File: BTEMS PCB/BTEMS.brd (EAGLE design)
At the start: 44.5 x 63.5 mm, 22 parts

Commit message: Solidified part position, added BOM
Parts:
- removed U$1: SDMMC06132, adafruit:06132
- added SDSLOT: SDMMC06132, adafruit:06132
- ARDUINO_A4-5, ARDUINO_A6-7: device SparkFun-Connectors:1X02_LOCK -> SparkFun-Connectors:1X02
- BAT_HEADER: device SparkFun-Connectors:SCREWTERMINAL-3.5MM-2_LOCK -> SparkFun-Connectors:1X02_2.54_SCREWTERM
- EXHEADER_A4-5, EXHEADER_A6-7: device SparkFun-Connectors:1X02 -> SparkFun-Connectors:1X02_LOCK
- I2C_R1, I2C_R2: value (none) -> 2.2k
- RTC_HEADER: device SparkFun-Connectors:1X04_LOCK -> SparkFun-Connectors:1X06_FEMALE_LOCK.010
- moved BAT_HEADER 54.5 mm to (4.19, 15.5)
- moved S1 42.1 mm to (3.68, 26.2), turned to 180 degrees
- moved MLX_HEADER 35.6 mm to (39.4, 2.54), turned to 180 degrees
- moved I2C_R2 25.0 mm to (20.3, 14.0), turned to 180 degrees
- moved ARDUINO_A6-7 24.1 mm to (30.6, 22.5)
- moved EXHEADER_A0-3 21.7 mm to (11.4, 27.9)
- moved EXHEADER_D2-9 21.7 mm to (11.4, 7.62)
- moved RED_LED 18.8 mm to (43.6, 26.3), turned to 90 degrees
- moved GREEN_LED 18.7 mm to (47.9, 26.3), turned to 90 degrees
- moved ARDUINO_A0-3 17.0 mm to (11.4, 25.4)
- moved ARDUINO_D2-9 17.0 mm to (11.4, 10.2)
- moved R3 16.6 mm to (35.4, 31.8), turned to 180 degrees
- moved R4 16.2 mm to (45.0, 31.8), turned to 180 degrees
- moved I2C_R1 15.5 mm to (30.5, 14.0), turned to 0 degrees
- moved EXHEADER_A6-7 11.5 mm to (24.1, 2.54), turned to 90 degrees
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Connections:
- net 3.3V: now also RTC_HEADER.2, RTC_HEADER.5, SDSLOT.4; no longer U$1.4
- net BAT_IN: now also BAT_HEADER.P2; no longer BAT_HEADER.2
- net D11: now also SDSLOT.2; no longer U$1.2
- net D12: now also SDSLOT.7; no longer U$1.7
- net D13: now also SDSLOT.5; no longer U$1.5
- net D4: now also SDSLOT.1; no longer U$1.1
- net GND: now also BAT_HEADER.P1, RTC_HEADER.6, SDSLOT.3, SDSLOT.6, SDSLOT.GP, SDSLOT.GP3; no longer BAT_HEADER.1, U$1.3, U$1.6, U$1.GP, U$1.GP3
- net VCC: no longer RTC_HEADER.2
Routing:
- net RST: track 5.08 -> 0.00 mm
- net GND: track 5.08 -> 0.00 mm
- net RXI: track 2.67 -> 0.00 mm
- net D9: track 2.67 -> 0.00 mm
- net D7: track 2.67 -> 0.00 mm
- net D5: track 2.67 -> 0.00 mm
- net D3: track 2.67 -> 0.00 mm
- net RAW: track 2.67 -> 0.00 mm
- net D13: track 2.67 -> 0.00 mm
- net D11: track 2.67 -> 0.00 mm
- net A3: track 2.67 -> 0.00 mm
- net A1: track 2.67 -> 0.00 mm
- net TXO: track 2.41 -> 0.00 mm
- net D8: track 2.41 -> 0.00 mm
- net D6: track 2.41 -> 0.00 mm
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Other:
- board size 44.5 x 63.5 mm -> 50.8 x 63.5 mm

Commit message: Routed board
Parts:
- moved EXHEADER_A6-7 26.1 mm to (43.2, 20.3), turned to 270 degrees
- moved SHT_HEADER 7.62 mm to (19.1, 2.54), turned to 180 degrees
- moved MLX_HEADER 7.62 mm to (31.8, 2.54), turned to 0 degrees
- moved EXHEADER_A4-5 2.54 mm to (26.7, 5.08), turned to 180 degrees
- moved BAT_HEADER 2.54 mm to (4.19, 18.0), turned to 270 degrees
- moved R_RLED 2.54 mm to (46.1, 19.1)
- moved R_GLED 0.46 mm to (48.3, 19.1)
- turned S1 to 0 degrees
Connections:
- removed net VCC: EXHEADER_A0-3.4
- new net RST2: ARDUINO_D2-9.3, EXHEADER_D2-9.3
- net 3.3V: now also EXHEADER_A0-3.4
- net BAT_IN: no longer R3.2
- net D10: now also SDSLOT.1
- net D4: no longer SDSLOT.1
- net RAW: now also R3.2
- net RST: no longer ARDUINO_D2-9.3, EXHEADER_D2-9.3
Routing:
- net SDA: track 0.00 -> 157.2 mm, vias 0 -> 1
- net SCL: track 0.00 -> 151.9 mm, vias 0 -> 1
- net GND: track 0.00 -> 60.7 mm, vias 0 -> 2
- net D12: track 0.00 -> 34.8 mm
- net D11: track 0.00 -> 33.1 mm, vias 0 -> 1
- net RAW: track 0.00 -> 32.9 mm
- net D13: track 0.00 -> 32.5 mm, vias 0 -> 2
- net A3: track 0.00 -> 25.4 mm
- net D10: track 0.00 -> 21.8 mm
- net D6: track 0.00 -> 21.2 mm
- net A7: track 0.00 -> 15.9 mm
- net D9: track 0.00 -> 15.7 mm
- net A6: track 0.00 -> 11.6 mm
- net BAT_IN: track 0.00 -> 5.80 mm
- net N$3: track 0.00 -> 3.43 mm
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- added copper zone on layer 1, net 3.3V
- added copper zone on layer 16, net GND

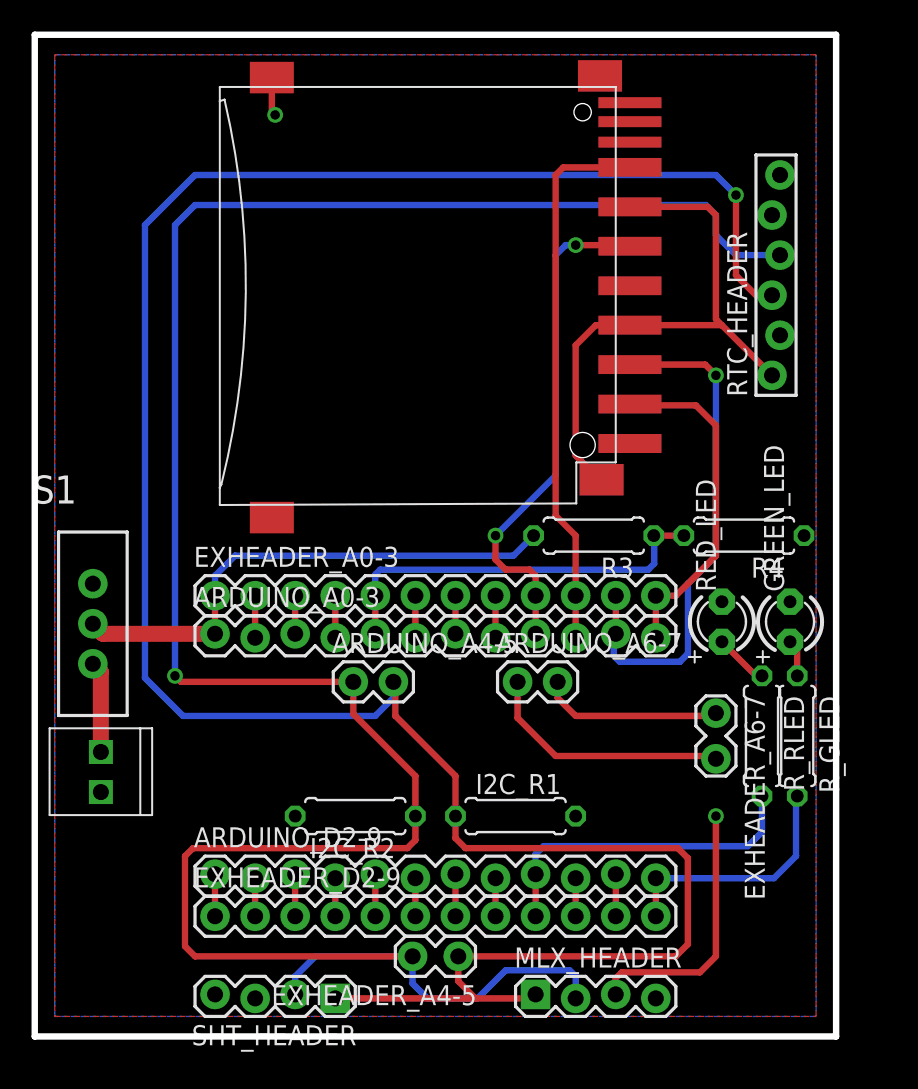
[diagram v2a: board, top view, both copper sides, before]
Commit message: Added silkscreen, BOM parts
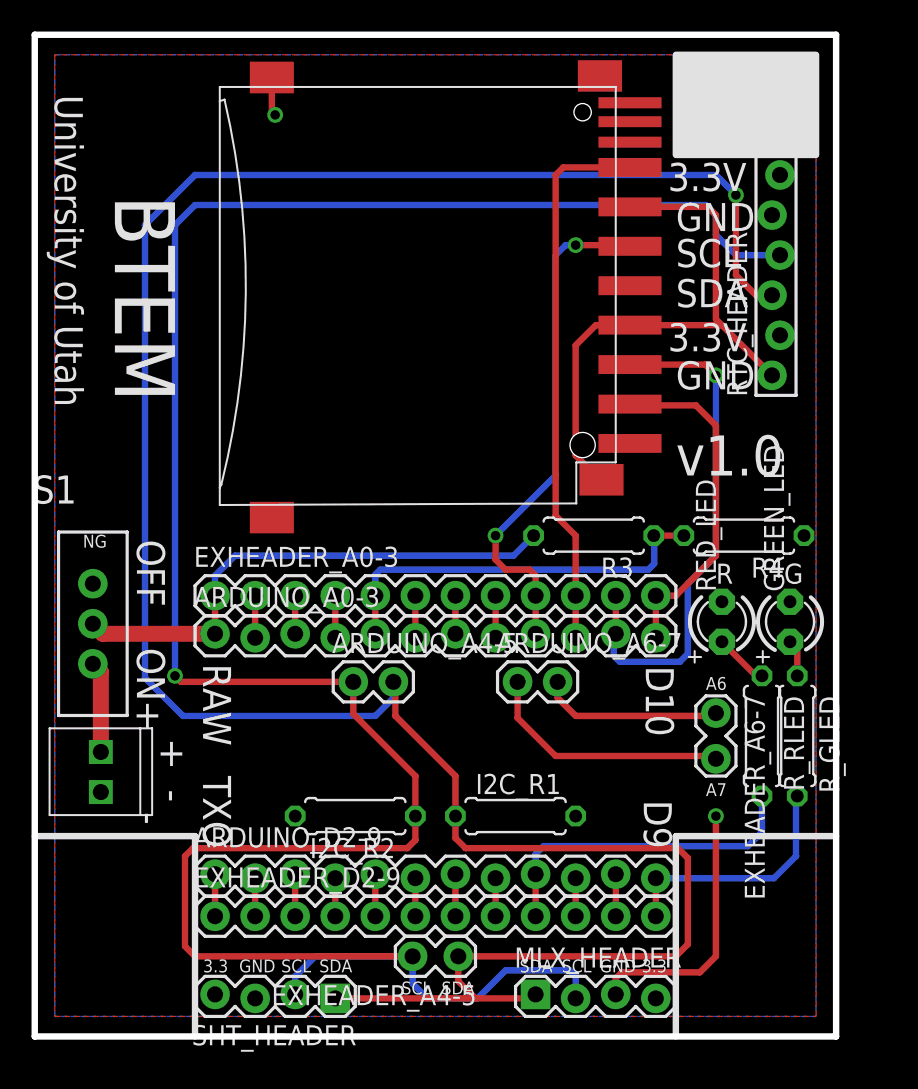
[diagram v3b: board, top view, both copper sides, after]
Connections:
- net 3.3V: now also RTC_HEADER.6; no longer RTC_HEADER.5
- net GND: now also RTC_HEADER.5; no longer RTC_HEADER.6
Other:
- board text added: "+"
- board text added: "-"
- board text added: "3.3"
- board text added: "3.3V"
- board text added: "A6"
- board text added: "A7"
- board text added: "BTEM"
- board text added: "D10"
- board text added: "D9"
- board text added: "G"
- board text added: "GND"
- board text added: "NG"
- board text added: "OFF"
- board text added: "ON"
- board text added: "R"
- board text added: "RAW"
- board text added: "SCL"
- board text added: "SDA"
- board text added: "TXO"
- board text added: "University of Utah"
- board text added: "v1.0"
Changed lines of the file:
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@@
 <wire x1="50.8" y1="63.5" x2="50.8" y2="0" width="0.4064" layer="20"/>
 <wire x1="50.8" y1="0" x2="0" y2="0" width="0.4064" layer="20"/>
-<wire x1="0" y1="0" x2="10.16" y2="0" width="0.4064" layer="49"/>
-<wire x1="10.16" y1="0" x2="40.64" y2="0" width="0.4064" layer="49"/>
-<wire x1="40.64" y1="0" x2="76.2" y2="0" width="0.4064" layer="49"/>
+<wire x1="0" y1="0" x2="76.2" y2="0" width="0.4064" layer="49"/>
 <wire x1="76.2" y1="0" x2="76.2" y2="127" width="0.4064" layer="49"/>
 <wire x1="76.2" y1="127" x2="0" y2="127" width="0.4064" layer="49"/>
-<wire x1="0" y1="127" x2="0" y2="12.7" width="0.4064" layer="49"/>
-<wire x1="0" y1="12.7" x2="0" y2="0" width="0.4064" layer="49"/>
-<wire x1="0" y1="12.7" x2="10.16" y2="12.7" width="0.4064" layer="49"/>
-<wire x1="10.16" y1="12.7" x2="10.16" y2="0" width="0.4064" layer="49"/>
-<wire x1="50.8" y1="12.7" x2="40.64" y2="12.7" width="0.4064" layer="49"/>
-<wire x1="40.64" y1="12.7" x2="40.64" y2="0" width="0.4064" layer="49"/>
+<wire x1="0" y1="127" x2="0" y2="0" width="0.4064" layer="49"/>
+<wire x1="0" y1="12.7" x2="10.16" y2="12.7" width="0.4064" layer="21"/>
+<wire x1="10.16" y1="12.7" x2="10.16" y2="0" width="0.4064" layer="21"/>
+<wire x1="50.8" y1="12.7" x2="40.64" y2="12.7" width="0.4064" layer="21"/>
+<wire x1="40.64" y1="12.7" x2="40.64" y2="0" width="0.4064" layer="21"/>
 <wire x1="49.53" y1="36.83" x2="49.53" y2="59.69" width="0.4064" layer="49"/>
+<text x="7.747" y="17.145" size="1.778" layer="21">+</text>
+<text x="6.223" y="19.558" size="1.778" layer="21">+</text>
+<text x="9.271" y="14.859" size="1.778" layer="21" rot="R90">-</text>
+<text x="5.969" y="14.224" size="1.778" layer="21" rot="R270">-</text>
+<text x="6.477" y="31.496" size="1.778" layer="21" rot="SR270">OFF</text>
+<text x="6.477" y="24.638" size="1.778" layer="21" rot="SR270">ON</text>
+<text x="1.27" y="59.69" size="1.778" layer="21" rot="SR270">University of Utah</text>
+<text x="5.08" y="53.34" size="3.81" layer="21" rot="SR270">BTEM</text>
+<text x="40.64" y="41.021" size="1.778" layer="21">GND</text>
+<text x="40.64" y="51.054" size="1.778" layer="21">GND</text>
+<text x="40.132" y="53.594" size="1.778" layer="21">3.3V</text>
+<text x="40.132" y="43.434" size="1.778" layer="21">3.3V</text>
+<text x="40.64" y="48.768" size="1.778" layer="21">SCL</text>
+<text x="40.64" y="46.228" size="1.778" layer="21">SDA</text>
+<text x="43.18" y="28.702" size="1.27" layer="21">R</text>
+<text x="47.498" y="28.702" size="1.27" layer="21">G</text>
+<text x="10.668" y="16.51" size="1.778" layer="21" rot="SR270">TXO</text>
+<text x="10.668" y="23.622" size="1.778" layer="21" rot="SR270">RAW</text>
+<text x="38.608" y="14.986" size="1.778" layer="21" rot="SR270">D9</text>
+<text x="38.735" y="23.495" size="1.778" layer="21" rot="SR270">D10</text>
+<text x="12.954" y="4.064" size="0.8128" layer="21">GND</text>
+<text x="35.814" y="4.064" size="0.8128" layer="21">GND</text>
+<text x="10.668" y="4.064" size="0.8128" layer="21">3.3</text>
+<text x="38.481" y="4.064" size="0.8128" layer="21">3.3</text>
+<text x="15.621" y="4.064" size="0.8128" layer="21">SCL</text>
+<text x="33.401" y="4.064" size="0.8128" layer="21">SCL</text>
+<text x="18.034" y="4.064" size="0.8128" layer="21">SDA</text>
+<text x="30.734" y="4.064" size="0.8128" layer="21">SDA</text>
+<text x="23.241" y="2.667" size="0.8128" layer="21">SCL</text>
+<text x="25.781" y="2.667" size="0.8128" layer="21">SDA</text>
+<text x="42.545" y="21.971" size="0.8128" layer="21">A6</text>
+<text x="42.545" y="15.24" size="0.8128" layer="21">A7</text>
+<text x="3.048" y="30.988" size="0.8128" layer="21">NG</text>
+<polygon width="0.4064" layer="21">
+<vertex x="40.64" y="62.23"/>
+<vertex x="49.53" y="62.23"/>
+<vertex x="49.53" y="55.88"/>
+<vertex x="40.64" y="55.88"/>
+</polygon>
+<text x="40.64" y="35.56" size="2.54" layer="21">v1.0</text>
 </plain>
 <attributes>
@@
 <element name="BAT_HEADER" library="SparkFun-Connectors" package="1X02_2.54_SCREWTERM" value="" x="4.191" y="18.034" locked="yes" rot="R270"/>
 <element name="EXHEADER_A0-3" library="SparkFun-Connectors" package="1X12" value="" x="11.43" y="27.94" locked="yes"/>
-<element name="EXHEADER_A4-5" library="SparkFun-Connectors" package="1X02_LOCK" value="" x="26.67" y="5.08" rot="R180"/>
-<element name="EXHEADER_A6-7" library="SparkFun-Connectors" package="1X02_LOCK" value="" x="43.18" y="20.32" rot="R270"/>
+<element name="EXHEADER_A4-5" library="SparkFun-Connectors" package="1X02_LOCK" value="" x="26.67" y="5.08" locked="yes" rot="R180"/>
+<element name="EXHEADER_A6-7" library="SparkFun-Connectors" package="1X02_LOCK" value="" x="43.18" y="20.32" locked="yes" rot="R270"/>
 <element name="EXHEADER_D2-9" library="SparkFun-Connectors" package="1X12" value="" x="11.43" y="7.62" locked="yes"/>
 <element name="GREEN_LED" library="adafruit" package="LED3MM" value="" x="47.879" y="26.289" locked="yes" rot="R90"/>
@@
 <element name="R3" library="adafruit" package="0207/7" value="24k" x="35.433" y="31.75" locked="yes" rot="R180"/>
 <element name="R4" library="adafruit" package="0207/7" value="30k" x="44.958" y="31.75" locked="yes" rot="R180"/>
-<element name="R_GLED" library="adafruit" package="0207/7" value="" x="48.3362" y="19.05" rot="R270"/>
-<element name="R_RLED" library="adafruit" package="0207/7" value="" x="46.101" y="19.05" rot="R270"/>
+<element name="R_GLED" library="adafruit" package="0207/7" value="" x="48.3362" y="19.05" locked="yes" rot="R270"/>
+<element name="R_RLED" library="adafruit" package="0207/7" value="" x="46.101" y="19.05" locked="yes" rot="R270"/>
 <element name="RED_LED" library="adafruit" package="LED3MM" value="" x="43.561" y="26.289" locked="yes" rot="R90"/>
 <element name="S1" library="SparkFun-Electromechanical" package="SWITCH-SPDT" value="" x="3.683" y="26.162" locked="yes">
@@
 <contactref element="GREEN_LED" pad="K"/>
 <contactref element="RED_LED" pad="K"/>
-<contactref element="RTC_HEADER" pad="6"/>
 <contactref element="RTC_HEADER" pad="1"/>
 <wire x1="13.97" y1="25.273" x2="13.97" y2="27.94" width="0.4064" layer="1"/>
@@
 <wire x1="42.164" y1="4.064" x2="43.18" y2="5.08" width="0.4064" layer="1"/>
 <wire x1="43.18" y1="5.08" x2="43.18" y2="13.97" width="0.4064" layer="1"/>
+<contactref element="RTC_HEADER" pad="5"/>
 </signal>
 <signal name="D2">
@@
 <contactref element="MLX_HEADER" pad="4"/>
 <contactref element="SHT_HEADER" pad="4"/>
-<contactref element="RTC_HEADER" pad="5"/>
 <contactref element="RTC_HEADER" pad="2"/>
 <contactref element="EXHEADER_A0-3" pad="4"/>
@@
 <vertex x="1.27" y="62.23"/>
 </polygon>
+<contactref element="RTC_HEADER" pad="6"/>
 </signal>
 <signal name="BAT_IN">

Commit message: Many changes and added gerber files
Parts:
- R1: value 24k -> R1
- R2: value 30k -> R2
- R_GLED: value (none) -> 220
- R_RLED: value (none) -> 270
- renumbered R3 to R1, R4 to R2
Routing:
- net GND: track 60.7 -> 51.0 mm, vias 2 -> 3
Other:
- board text added: "BTEMS"
- board text added: "Environmental Fluid Dynamics Lab"
- board text removed: "BTEM"
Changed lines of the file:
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@@
 <text x="6.477" y="31.496" size="1.778" layer="21" rot="SR270">OFF</text>
 <text x="6.477" y="24.638" size="1.778" layer="21" rot="SR270">ON</text>
-<text x="1.27" y="59.69" size="1.778" layer="21" rot="SR270">University of Utah</text>
-<text x="5.08" y="53.34" size="3.81" layer="21" rot="SR270">BTEM</text>
+<text x="2.54" y="54.61" size="1.016" layer="21" rot="SR270">University of Utah</text>
+<text x="6.35" y="55.245" size="3.81" layer="1" rot="SR270">BTEMS</text>
 <text x="40.64" y="41.021" size="1.778" layer="21">GND</text>
 <text x="40.64" y="51.054" size="1.778" layer="21">GND</text>
@@
 </polygon>
 <text x="40.64" y="35.56" size="2.54" layer="21">v1.0</text>
+<text x="1.27" y="60.325" size="1.016" layer="21" rot="SR270">Environmental Fluid Dynamics Lab</text>
 </plain>
 <attributes>
@@
 <element name="I2C_R1" library="adafruit" package="0207/7" value="2.2k" x="30.48" y="13.97" locked="yes"/>
 <element name="I2C_R2" library="adafruit" package="0207/7" value="2.2k" x="20.32" y="13.97" locked="yes" rot="R180"/>
-<element name="R3" library="adafruit" package="0207/7" value="24k" x="35.433" y="31.75" locked="yes" rot="R180"/>
-<element name="R4" library="adafruit" package="0207/7" value="30k" x="44.958" y="31.75" locked="yes" rot="R180"/>
-<element name="R_GLED" library="adafruit" package="0207/7" value="" x="48.3362" y="19.05" locked="yes" rot="R270"/>
-<element name="R_RLED" library="adafruit" package="0207/7" value="" x="46.101" y="19.05" locked="yes" rot="R270"/>
+<element name="R1" library="adafruit" package="0207/7" value="R1" x="35.433" y="31.75" locked="yes" rot="R180"/>
+<element name="R2" library="adafruit" package="0207/7" value="R2" x="44.958" y="31.75" locked="yes" rot="R180"/>
+<element name="R_GLED" library="adafruit" package="0207/7" value="220" x="48.3362" y="19.05" locked="yes" rot="R270"/>
+<element name="R_RLED" library="adafruit" package="0207/7" value="270" x="46.101" y="19.05" locked="yes" rot="R270"/>
 <element name="RED_LED" library="adafruit" package="LED3MM" value="" x="43.561" y="26.289" locked="yes" rot="R90"/>
 <element name="S1" library="SparkFun-Electromechanical" package="SWITCH-SPDT" value="" x="3.683" y="26.162" locked="yes">
@@
 <contactref element="SHT_HEADER" pad="3"/>
 <contactref element="BAT_HEADER" pad="P1"/>
-<contactref element="R4" pad="1"/>
+<contactref element="R2" pad="1"/>
 <contactref element="GREEN_LED" pad="K"/>
 <contactref element="RED_LED" pad="K"/>
@@
 <wire x1="13.97" y1="25.273" x2="13.97" y2="27.94" width="0.4064" layer="1"/>
 <wire x1="19.05" y1="7.62" x2="19.05" y2="10.033" width="0.4064" layer="1"/>
-<wire x1="35.93" y1="35.29" x2="35.83" y2="35.29" width="0.4064" layer="1"/>
-<wire x1="35.83" y1="35.29" x2="34.29" y2="36.83" width="0.4064" layer="1"/>
-<wire x1="34.29" y1="36.83" x2="34.29" y2="43.815" width="0.4064" layer="1"/>
-<wire x1="34.29" y1="43.815" x2="35.56" y2="45.085" width="0.4064" layer="1"/>
-<wire x1="35.56" y1="45.085" x2="37.725" y2="45.085" width="0.4064" layer="1"/>
-<wire x1="37.725" y1="45.085" x2="37.73" y2="45.09" width="0.4064" layer="1"/>
 <wire x1="37.73" y1="45.09" x2="43.556" y2="45.09" width="0.4064" layer="1"/>
 <wire x1="43.556" y1="45.09" x2="46.736" y2="41.91" width="0.4064" layer="1"/>
@@
 <wire x1="43.18" y1="5.08" x2="43.18" y2="13.97" width="0.4064" layer="1"/>
 <contactref element="RTC_HEADER" pad="5"/>
+<via x="39.37" y="35.179" extent="1-16" drill="0.6" shape="square"/>
+<wire x1="35.93" y1="35.29" x2="39.37" y2="35.29" width="0.4064" layer="1"/>
+<wire x1="39.37" y1="35.29" x2="39.37" y2="35.179" width="0.4064" layer="1"/>
 </signal>
 <signal name="D2">
@@
 <wire x1="11.43" y1="25.527" x2="4.318" y2="25.527" width="1.016" layer="1"/>
 <wire x1="4.318" y1="25.527" x2="3.683" y2="26.162" width="1.016" layer="1"/>
-<contactref element="R3" pad="2"/>
+<contactref element="R1" pad="2"/>
 <wire x1="11.43" y1="27.94" x2="11.43" y2="29.21" width="0.4064" layer="16"/>
 <wire x1="11.43" y1="29.21" x2="12.7" y2="30.48" width="0.4064" layer="16"/>
@@
 <contactref element="ARDUINO_A0-3" pad="5"/>
 <contactref element="EXHEADER_A0-3" pad="5"/>
-<contactref element="R3" pad="1"/>
-<contactref element="R4" pad="2"/>
+<contactref element="R1" pad="1"/>
+<contactref element="R2" pad="2"/>
 <wire x1="21.59" y1="25.527" x2="21.59" y2="27.94" width="0.4064" layer="1"/>
 <wire x1="39.243" y1="31.75" x2="41.148" y2="31.75" width="0.4064" layer="1"/>
